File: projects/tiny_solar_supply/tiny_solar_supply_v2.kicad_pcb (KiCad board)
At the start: 2 copper layers, 36.8 x 20.8 mm, 20 parts, among them J1 Conn_01x02, J2 Conn_01x02, J3 Conn_01x02, J4 Conn_01x02, T1 2N7002 (SOT-23), U1 AP3015AKTR-G1

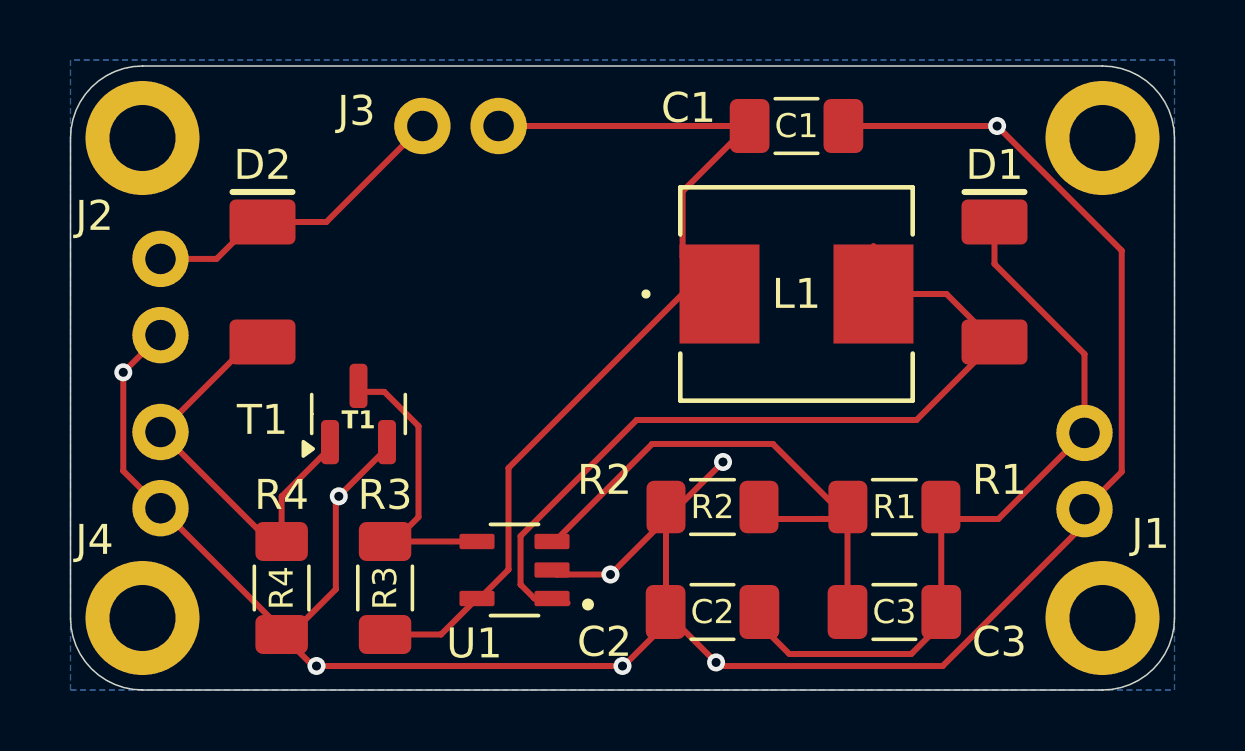
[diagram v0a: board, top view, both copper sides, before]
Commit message: Add details to tiny_solar_supply
Improve silkscreen
add logo title and version v1.0
replace header pins by slide switch

NOTE: broken link to shematic (tiny_solar_supply_v2.kicad_sch does not exist!)
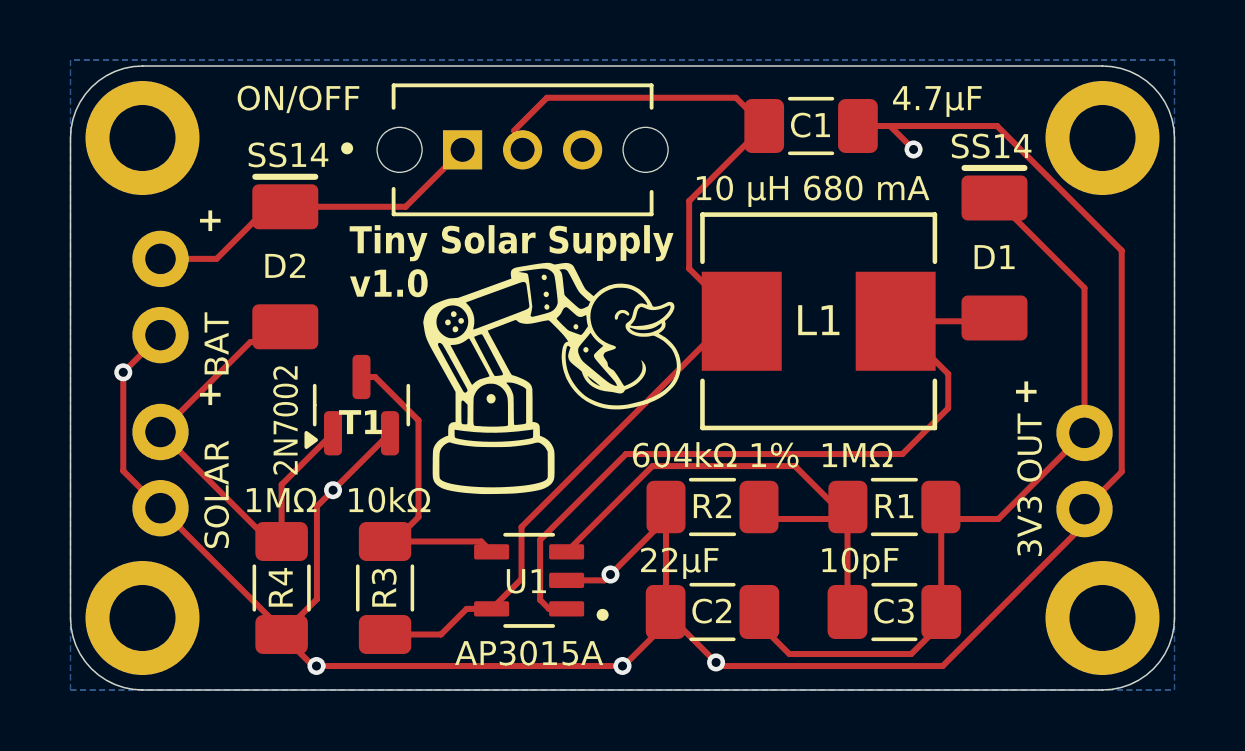
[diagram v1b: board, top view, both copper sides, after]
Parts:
- added G***: LOGO, MH_logo:robot_duckie_logo_10mm, F.Cu at (146.0, 94.2)
- C1: value 4.7 µF, 50 V, X7R (0805) -> 4.7µF
- C2: value 22 µF, 10 V, X7R (1206) -> 22µF
- C3: value 10 pF, 50 V, X7R (0805) -> 10pF
- D1, D2: value SS14 (DO-214AC) -> SS14
- J3: footprint SparkFun-Connector:1x02 -> MH_Slide_Switch:SW_OS102011MS2QN1
- L1: value 10 µH, 680 mA -> 10 µH 680 mA
- R1, R4: value 1 MΩ (0805, 0.125 W) -> 1MΩ
- R2: value 604 kΩ, 1% (0805, 0.125 W) -> 604kΩ 1%
- R3: value 10 kΩ (0805, 0.125 W) -> 10kΩ
- T1: value 2N7002 (SOT-23) -> 2N7002
- U1: value AP3015AKTR-G1 -> AP3015A
- moved J3 3.43 mm to (145.1, 87.0)
- moved L1 1.17 mm to (154.9, 92.7)
- moved D2 0.91 mm to (137.2, 90.9)
- moved D1 0.80 mm to (160.8, 90.6)
- moved U1 0.60 mm to (145.3, 101.3)
- moved C1 0.49 mm to (154.7, 86.2)
- moved T1 0.31 mm to (139.7, 95.5)
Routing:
- net Net-(D1-A): track 28.6 -> 25.4 mm
- net GNDD: track 83.1 -> 81.7 mm, vias 8 -> 7
- net Net-(J3-Pin_2): track 33.4 -> 34.7 mm
- net Net-(T1-D): track 10.5 -> 11.5 mm
- net Net-(U1-FB): track 18.7 -> 17.8 mm
- net /BATT_POSITIVE: track 10.6 -> 11.1 mm
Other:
- board text added: "+"
- board text added: "Tiny Solar Supply v1.0"
